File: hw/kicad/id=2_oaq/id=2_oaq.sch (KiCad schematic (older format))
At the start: 51 parts

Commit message: Update for OAQ
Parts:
- added C?: 10uF, Capacitors_SMD:C_0805, symbol C_Small
- added C? (x2): 100nF, symbol C_Small
- added Q?: ISL21080CIH325Z-TK, SOT95P237X112-3N, symbol ISL21080CIH325Z-TK
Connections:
- net 2V7: now also C?.1, C?.1, Q?.1 (VIN)
- net GND: now also C?.2, C?.2, C?.2, Q?.3 (GND)
- net CO_EN: now reaches IC?.A14 (P1.15)
- net NO2_EN: now reaches IC?.A16 (P1.13)
- net SO2_EN: now reaches IC?.B15 (P1.14)
- net O3_EN: now reaches IC?.B17 (P1.12)
- net SCL renamed OutdorAirQualitySensors/SCL
- net SDA renamed OutdorAirQualitySensors/SDA
- new net 2V5: C?.1, Q?.2 (VOUT)
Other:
- note added: "H2S_EN\n"
- note added: "Voltage Reference for LMP91000"
- note removed: "28.Jan.2018"
- note removed: "A"
- note removed: "Climate Outdoor Air Quality (O3, NO2, SO2, CO). Module ID=2."
- moved on the sheet: C?, IC?, R?

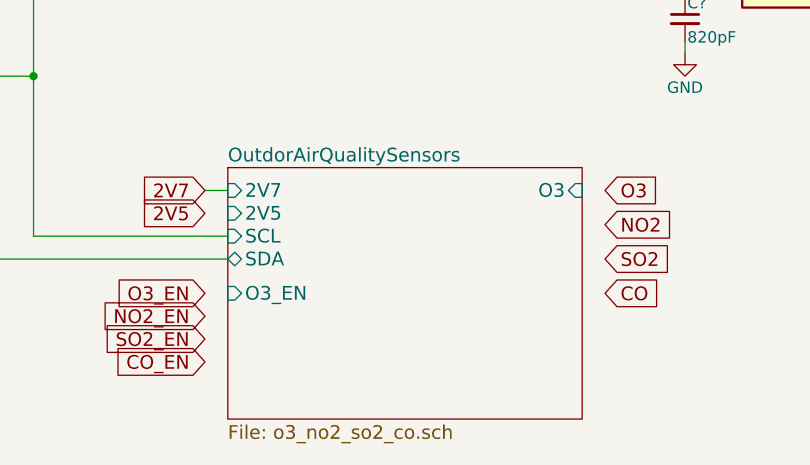
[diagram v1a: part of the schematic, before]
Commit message: OAQ schematic updated: gains, ranges
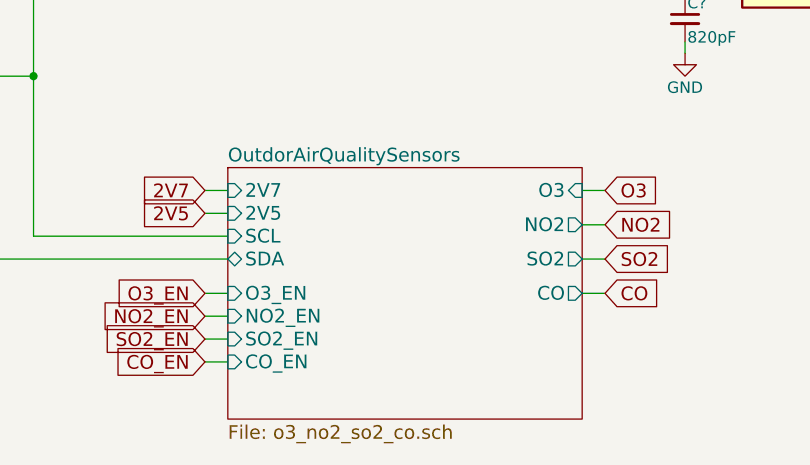
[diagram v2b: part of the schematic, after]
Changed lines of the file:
@@
 F6 "O3_EN" I L 3950 6850 60
 F7 "2V5" I L 3950 6500 60
+F8 "NO2" O R 5500 6550 60
+F9 "CO" O R 5500 6850 60
+F10 "SO2" O R 5500 6700 60
+F11 "SO2_EN" I L 3950 7050 60
+F12 "NO2_EN" I L 3950 6950 60
+F13 "CO_EN" I L 3950 7150 60
 $EndSheet
 Wire Wire Line
@@
 Connection ~ 3100 5900
 Connection ~ 2750 5700
+Wire Wire Line
+	3850 6500 3950 6500
+Wire Wire Line
+	3850 6850 3950 6850
+Wire Wire Line
+	3850 6950 3950 6950
+Wire Wire Line
+	3850 7050 3950 7050
+Wire Wire Line
+	3850 7150 3950 7150
+Wire Wire Line
+	5600 6850 5500 6850
+Wire Wire Line
+	5600 6700 5500 6700
+Wire Wire Line
+	5600 6550 5500 6550
+Wire Wire Line
+	5600 6400 5500 6400
 $EndSCHEMATC

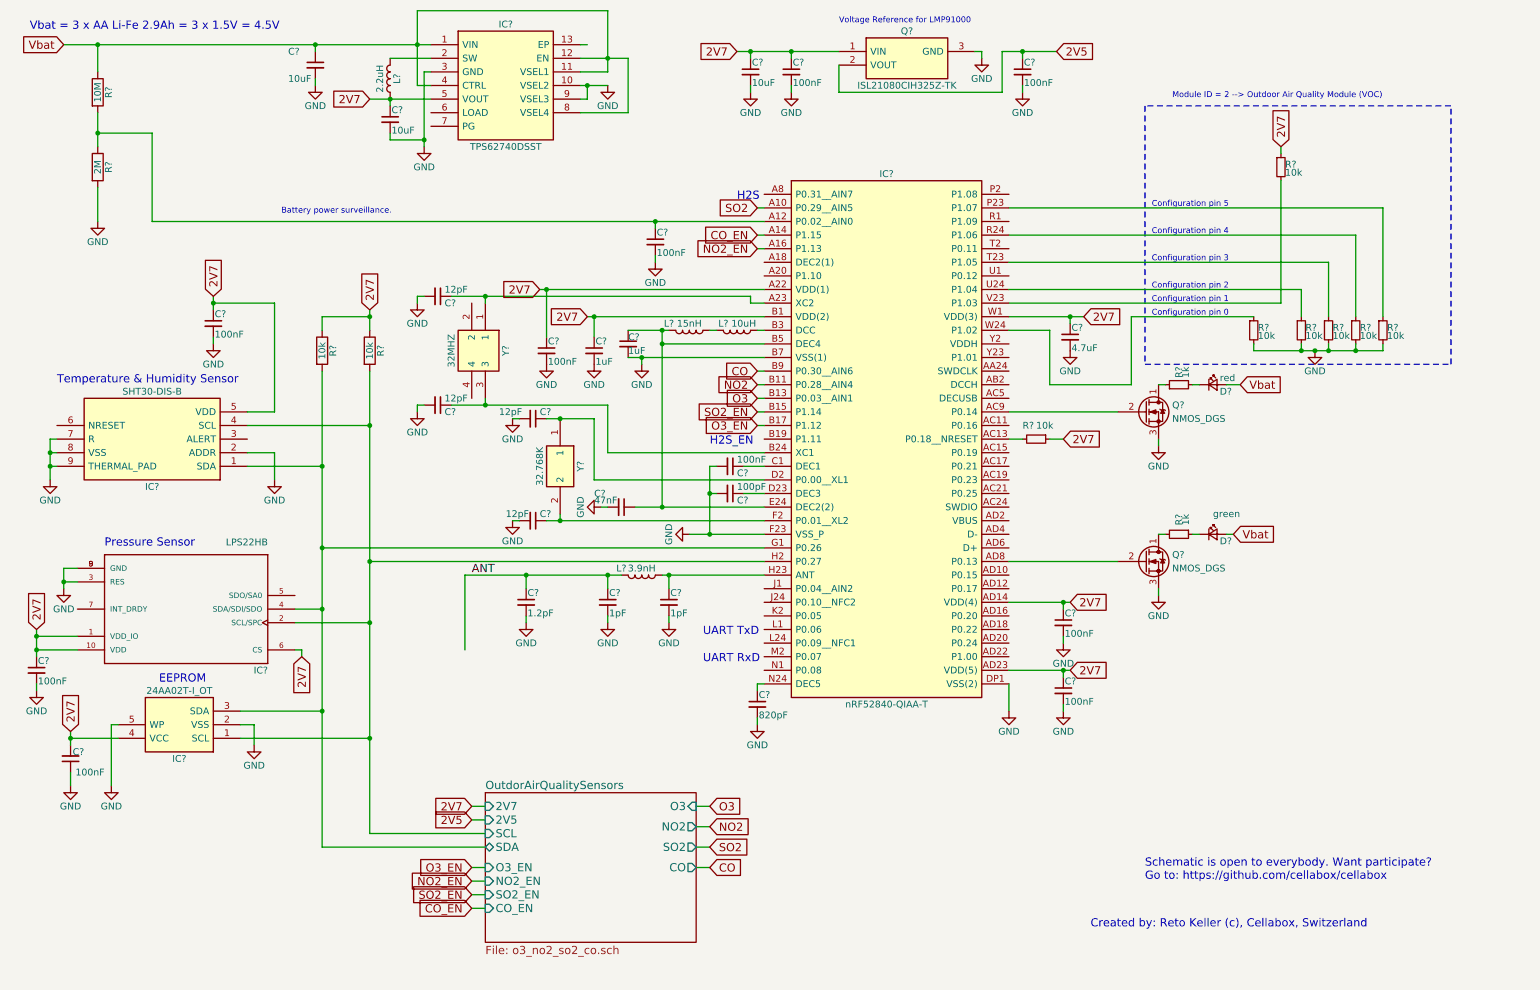
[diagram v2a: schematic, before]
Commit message: Indoor PM2.5 module. Schematic added.
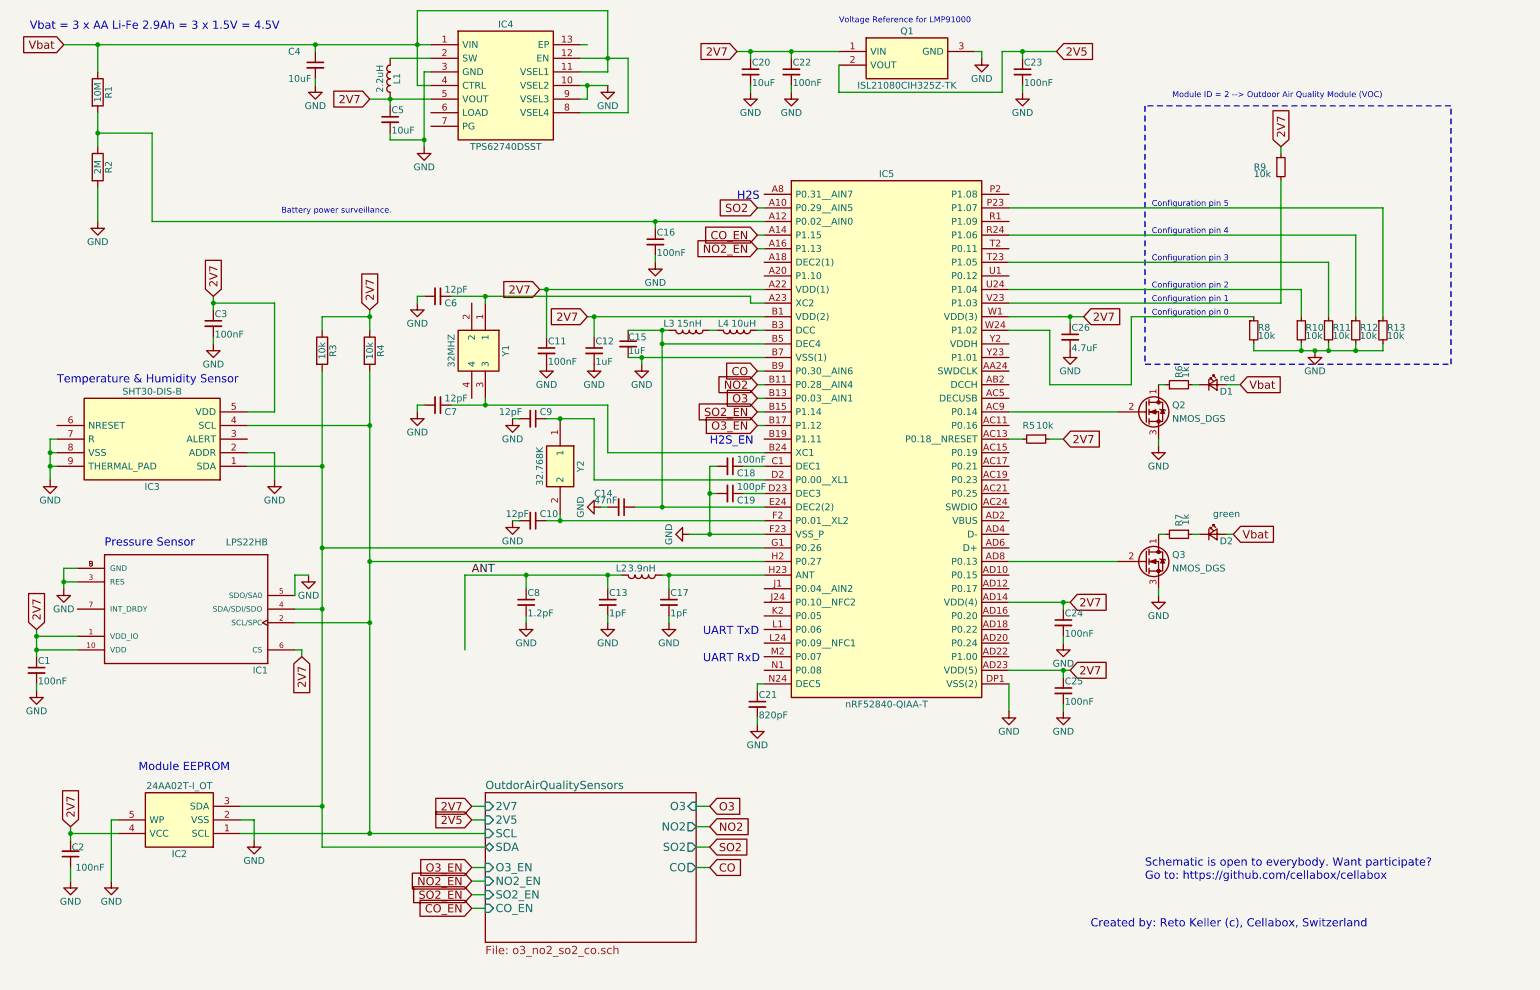
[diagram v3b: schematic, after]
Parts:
- gave numbers to parts that had none: 55
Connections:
- net GND: now also IC1.5 (SDO/SA0)
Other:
- note added: "Module EEPROM"
- note removed: "EEPROM"
- moved on the sheet: C2, IC2

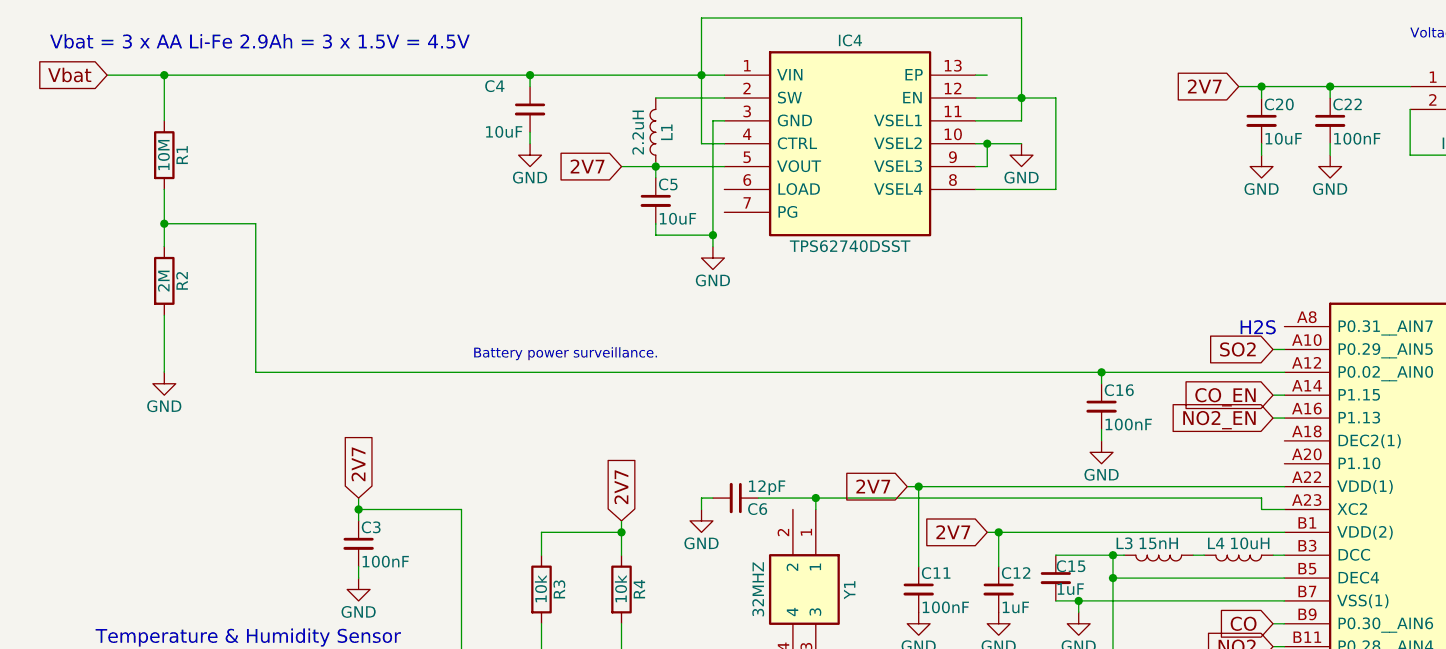
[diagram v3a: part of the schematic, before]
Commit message: Updated schematics: battery surveillance.
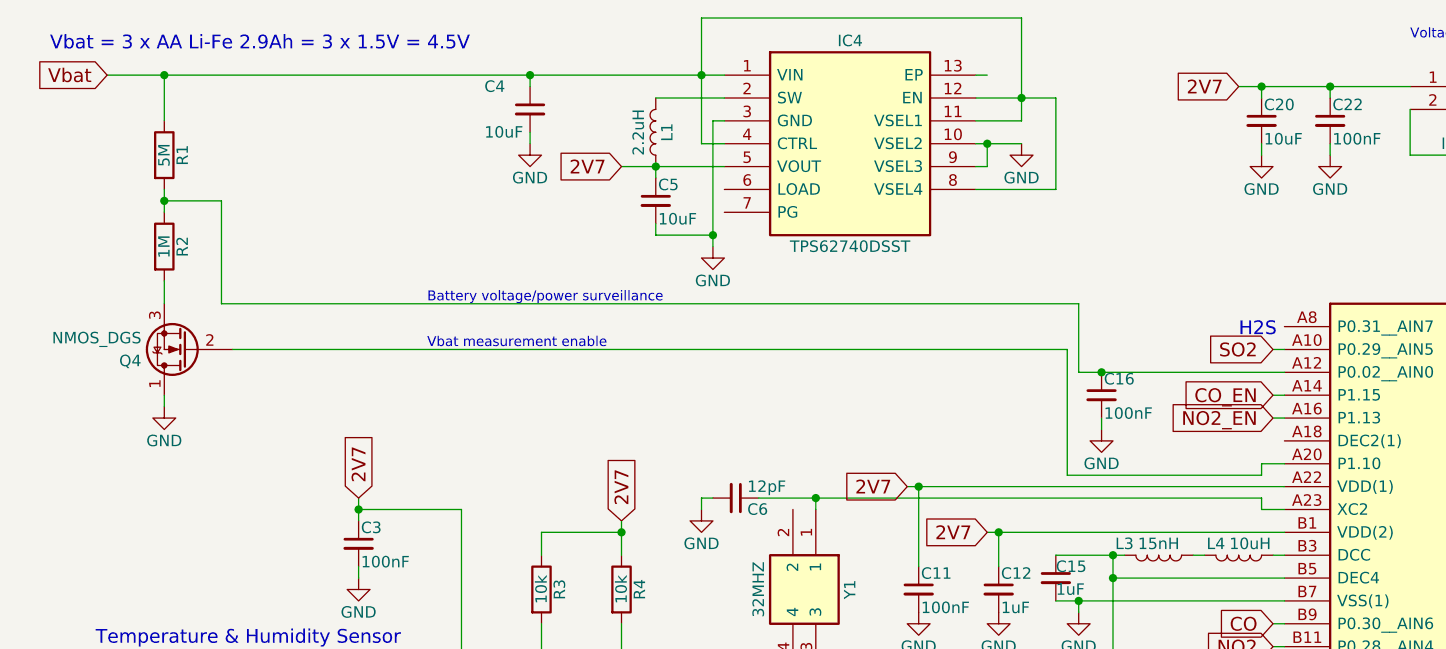
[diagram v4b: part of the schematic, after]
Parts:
- added Q4: NMOS_DGS, symbol Q_NMOS_DGS
- R1: value 10M -> 5M
- R2: value 2M -> 1M
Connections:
- net GND: now also Q4.1 (D); no longer R2.2
- net at IC5.A20 (P1.10): now also Q4.2 (G)
- new net: Q4.3 (S), R2.2
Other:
- note added: "Battery voltage/power surveillance"
- note added: "Vbat measurement enable"
- note removed: "Battery power surveillance."
- moved on the sheet: C16, R2
